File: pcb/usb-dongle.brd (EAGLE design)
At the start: 31.2 x 26.7 mm, 40 parts, among them IC1 STM32F103C8, IC2 TPS76333, IC3 NRF24L01-MOD-SMD, Q1 8MHz, SW1 KSS-2EG4430, X1 USB-MALE-A-H

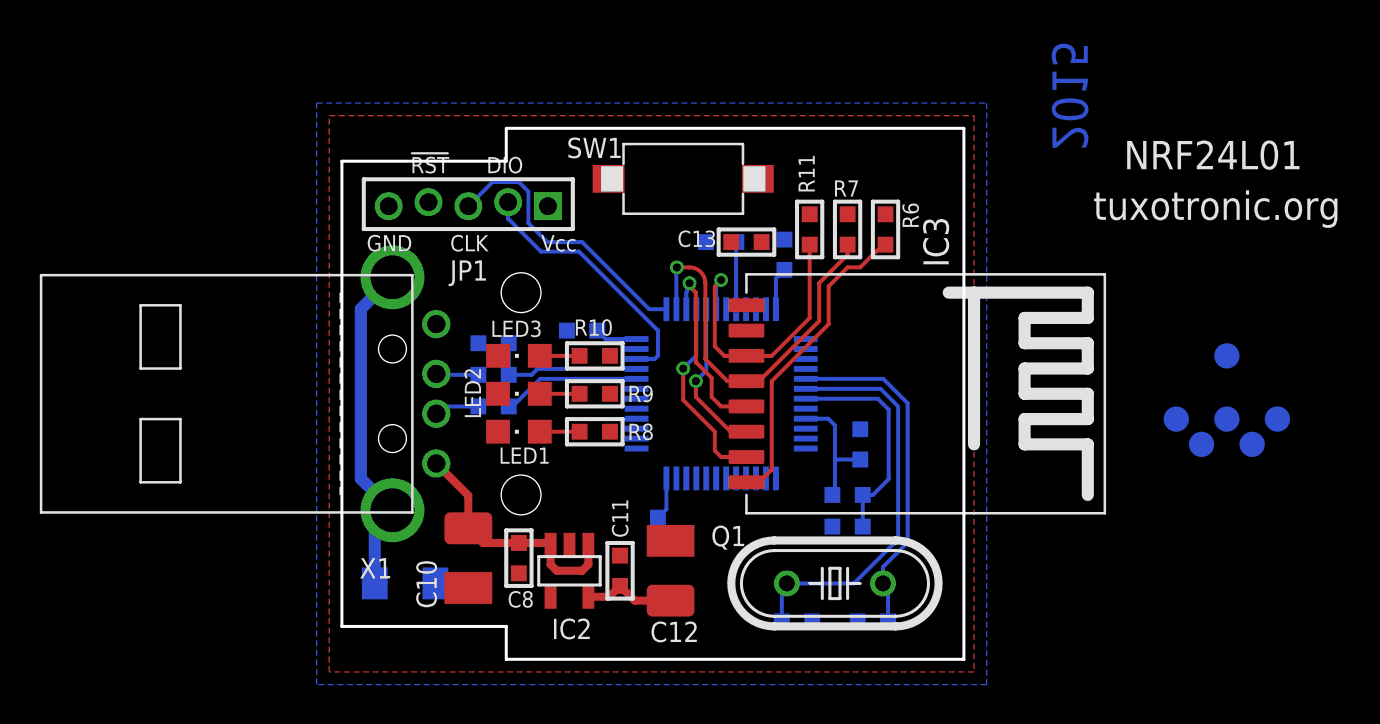
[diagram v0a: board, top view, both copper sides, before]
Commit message: USB-dongle. need review
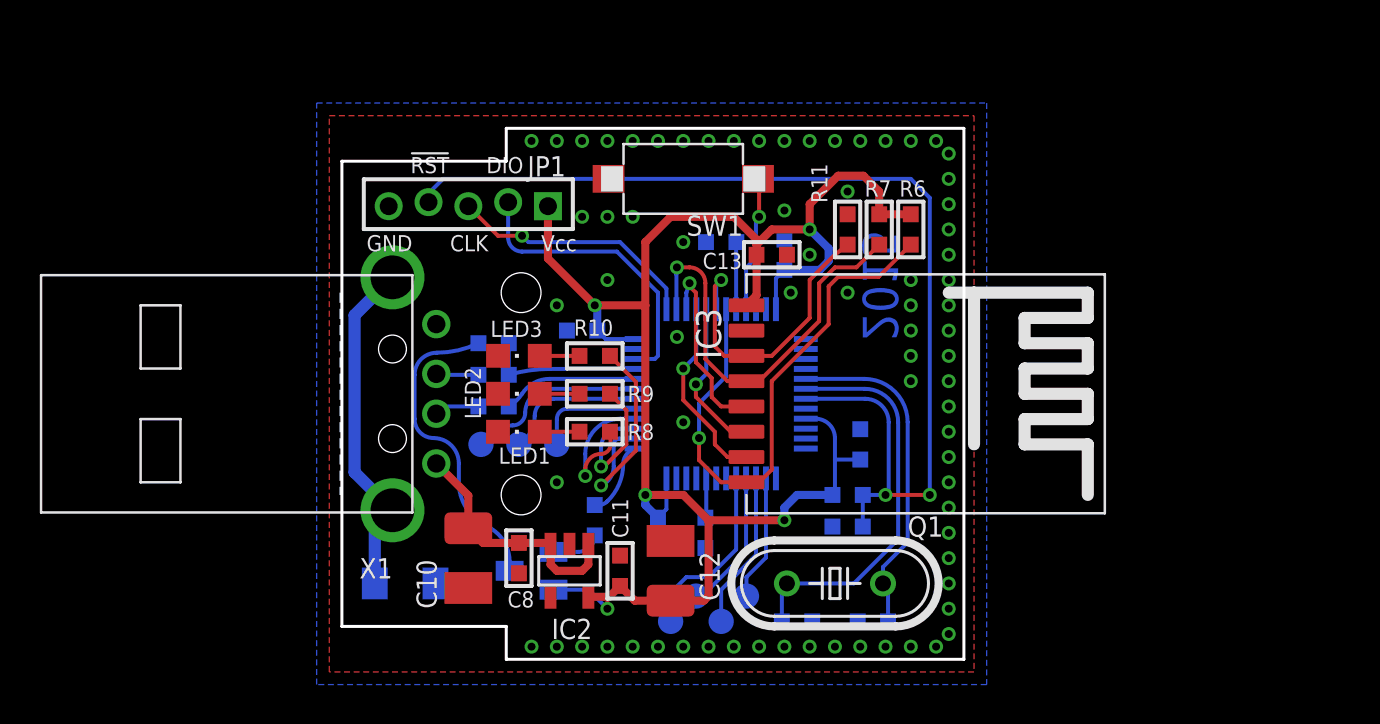
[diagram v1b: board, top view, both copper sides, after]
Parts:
- added Q2: (no value), semiconductor:SOT23
- added R12, R13: 10K, rc-master-smd:R0603
- added TP7: TPB1,27, testpad:B1,27
- moved TP2 38.7 mm to (6.99, 10.8)
- moved TP1 38.1 mm to (8.89, 10.8), turned to 0 degrees
- moved TP4 28.7 mm to (19.1, 1.91)
- moved TP6 28.1 mm to (16.5, 1.91)
- moved TP3 25.7 mm to (20.3, 3.17)
- moved TP5 25.7 mm to (17.8, 3.17)
- moved R11 1.90 mm to (25.4, 21.6)
- moved R7 1.59 mm to (27.0, 21.6)
- moved C13 1.42 mm to (21.6, 20.3)
- moved R6 1.27 mm to (28.6, 21.6)
- turned R3 to 0 degrees
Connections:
- new net !DISC: IC1.25, R13.1
- new net N$12: IC1.14, TP3.PP
- new net N$13: IC1.15, TP4.PP
- new net N$14: IC1.16, TP5.PP
- new net N$15: IC1.17, TP6.PP
- new net N$16: IC1.29, TP7.PP
- new net N$17: IC1.20, R12.1
- new net N$18: Q2.1, R13.2
- new net N$19: Q2.3, R3.2
- new net N$4: IC1.30, TP1.PP
- new net N$5: IC1.31, TP2.PP
- net !BUTTON: now also IC1.45
- net !RF_IRQ: now also IC1.43
- net +3V3: now also Q2.2
- net GND: now also R12.2
- net LED1: now also IC1.28
- net LED2: now also IC1.27
- net LED3: now also IC1.26
- net USB_DP: now also R3.1; no longer R3.2
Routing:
- net +3V3: track 17.5 -> 87.3 mm, vias 0 -> 5
- net !RESET: track 11.1 -> 54.6 mm, vias 0 -> 2
- net N$19: track 0.00 -> 15.3 mm
- net !RF_IRQ: track 15.6 -> 27.9 mm, vias 0 -> 1
- net LED3: track 0.00 -> 11.3 mm, vias 0 -> 1
- net N$15: track 0.00 -> 9.19 mm
- net N$5: track 0.00 -> 8.84 mm
- net N$13: track 0.00 -> 7.90 mm
- net LED2: track 0.00 -> 7.74 mm, vias 0 -> 1
- net LED1: track 0.00 -> 7.17 mm, vias 0 -> 1
- net N$14: track 0.00 -> 7.14 mm
- net N$4: track 0.00 -> 7.08 mm
- net !BUTTON: track 0.00 -> 6.84 mm, vias 0 -> 1
- net N$12: track 0.00 -> 6.32 mm
- net N$16: track 0.00 -> 5.49 mm
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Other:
- board text added: "NRF24L01 Rev.A"
- board text removed: "NRF24L01"
